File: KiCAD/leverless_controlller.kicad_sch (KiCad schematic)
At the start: 1 part

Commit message: Start PCB Layout
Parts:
- S1: footprint keyswitches.pretty-2.1:Stabilizer_MX_2u -> Fightstick_Library:Kailh_MX_Style_Keyswitch
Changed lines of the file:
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@@
-(kicad_sch (version 20230121) (generator eeschema)
-  (paper "A4")
-  (symbol (lib_id "Keyboard:Stabilizer_MX_2u") (at 49.53 149.86 0) (unit 1)
-    (in_bom no) (on_board yes) (dnp no) (fields_autoplaced)
-    (property "Reference" "S1" (at 59.69 154.305 0)
-      (effects (font (size 1.27 1.27)) (justify left))
-    )
-    (property "Value" "~" (at 49.53 149.86 0)
-      (effects (font (size 1.27 1.27)))
-    )
-    (property "Footprint" "keyswitches.pretty-2.1:Stabilizer_MX_2u" (at 49.53 149.86 0)
-      (effects (font (size 1.27 1.27)) hide)
-    )
-    (property "Datasheet" "" (at 49.53 149.86 0)
-      (effects (font (size 1.27 1.27)) hide)
-    )
-    (instances
-      (project "leverless_controlller"
-        (path "/d4101bc9-65c8-46ec-b973-5d64e4a94ac0"
-          (reference "S1") (unit 1)
-        )
-      )
-    )
-  )
-  (sheet (at 38.1 27.94) (size 64.77 67.31) (fields_autoplaced)
-    (stroke (width 0.1524) (type solid))
-    (fill (color 0 0 0 0.0000))
-    (property "Sheetname" "Main" (at 38.1 27.2284 0)
-      (effects (font (size 1.27 1.27)) (justify left bottom))
-    )
-    (property "Sheetfile" "Main.kicad_sch" (at 38.1 95.8346 0)
-      (effects (font (size 1.27 1.27)) (justify left top))
-    )
-    (instances
-      (project "leverless_controlller"
-        (path "/d4101bc9-65c8-46ec-b973-5d64e4a94ac0" (page "2"))
-      )
-    )
-  )
-  (sheet (at 142.24 29.21) (size 80.01 62.23) (fields_autoplaced)
-    (stroke (width 0.1524) (type solid))
-    (fill (color 0 0 0 0.0000))
-    (property "Sheetname" "Buttons" (at 142.24 28.4984 0)
-      (effects (font (size 1.27 1.27)) (justify left bottom))
-    )
-    (property "Sheetfile" "Buttons.kicad_sch" (at 142.24 92.0246 0)
-      (effects (font (size 1.27 1.27)) (justify left top))
-    )
-    (instances
-      (project "leverless_controlller"
-        (path "/d4101bc9-65c8-46ec-b973-5d64e4a94ac0" (page "3"))
-      )
-    )
-  )
-  (sheet_instances
-    (path "/" (page "1"))
-  )
+(kicad_sch
+	(version 20231120)
+	(generator "eeschema")
+	(generator_version "8.0")
+	(paper "A4")
+	(symbol
+		(lib_id "Keyboard:Stabilizer_MX_2u")
+		(at 49.53 149.86 0)
+		(unit 1)
+		(exclude_from_sim no)
+		(in_bom no)
+		(on_board yes)
+		(dnp no)
+		(fields_autoplaced yes)
+		(property "Reference" "S1"
+			(at 59.69 154.305 0)
+			(effects
+				(font
+					(size 1.27 1.27)
+				)
+				(justify left)
+			)
+		)
+		(property "Value" "~"
+			(at 49.53 149.86 0)
+			(effects
+				(font
+					(size 1.27 1.27)
+				)
+			)
+		)
+		(property "Footprint" "Fightstick_Library:Kailh_MX_Style_Keyswitch"
+			(at 49.53 149.86 0)
+			(effects
+				(font
+					(size 1.27 1.27)
+				)
+				(hide yes)
+			)
+		)
+		(property "Datasheet" ""
+			(at 49.53 149.86 0)
+			(effects
+				(font
+					(size 1.27 1.27)
+				)
+				(hide yes)
+			)
+		)
+		(property "Description" ""
+			(at 49.53 149.86 0)
+			(effects
+				(font
+					(size 1.27 1.27)
+				)
+				(hide yes)
+			)
+		)
+		(instances
+			(project "leverless_controlller"
+				(path "/d4101bc9-65c8-46ec-b973-5d64e4a94ac0"
+					(reference "S1")
+					(unit 1)
+				)
+			)
+		)
+	)
+	(sheet
+		(at 38.1 27.94)
+		(size 64.77 67.31)
+		(fields_autoplaced yes)
+		(stroke
+			(width 0.1524)
+			(type solid)
+		)
+		(fill
+			(color 0 0 0 0.0000)
+		)
+		(property "Sheetname" "Main"
+			(at 38.1 27.2284 0)
+			(effects
+				(font
+					(size 1.27 1.27)
+				)
+				(justify left bottom)
+			)
+		)
+		(property "Sheetfile" "Main.kicad_sch"
+			(at 38.1 95.8346 0)
+			(effects
+				(font
+					(size 1.27 1.27)
+				)
+				(justify left top)
+			)
+		)
+		(instances
+			(project "leverless_controlller"
+				(path "/d4101bc9-65c8-46ec-b973-5d64e4a94ac0"
+					(page "2")
+				)
+			)
+		)
+	)
+	(sheet
+		(at 142.24 29.21)
+		(size 80.01 62.23)
+		(fields_autoplaced yes)
+		(stroke
+			(width 0.1524)
+			(type solid)
+		)
+		(fill
+			(color 0 0 0 0.0000)
+		)
+		(property "Sheetname" "Buttons"
+			(at 142.24 28.4984 0)
+			(effects
+				(font
+					(size 1.27 1.27)
+				)
+				(justify left bottom)
+			)
+		)
+		(property "Sheetfile" "Buttons.kicad_sch"
+			(at 142.24 92.0246 0)
+			(effects
+				(font
+					(size 1.27 1.27)
+				)
+				(justify left top)
+			)
+		)
+		(instances
+			(project "leverless_controlller"
+				(path "/d4101bc9-65c8-46ec-b973-5d64e4a94ac0"
+					(page "3")
+				)
+			)
+		)
+	)
+	(sheet_instances
+		(path "/"
+			(page "1")
+		)
+	)
 )

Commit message: PCB First Draft
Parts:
- S1: footprint Fightstick_Library:Kailh_MX_Style_Keyswitch -> PCM_Mounting_Keyboard_Stabilizer:Stabilizer_Cherry_MX_2.00u
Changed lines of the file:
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@@
 			)
 		)
-		(property "Footprint" "Fightstick_Library:Kailh_MX_Style_Keyswitch"
+		(property "Footprint" "PCM_Mounting_Keyboard_Stabilizer:Stabilizer_Cherry_MX_2.00u"
 			(at 49.53 149.86 0)
 			(effects

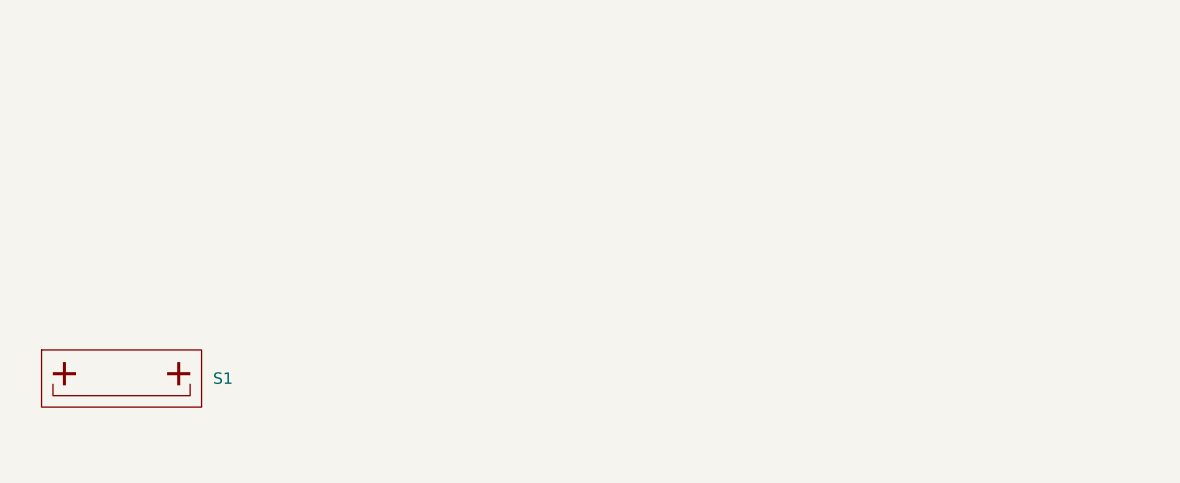
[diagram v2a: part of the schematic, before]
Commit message: Make PCB and case fit together
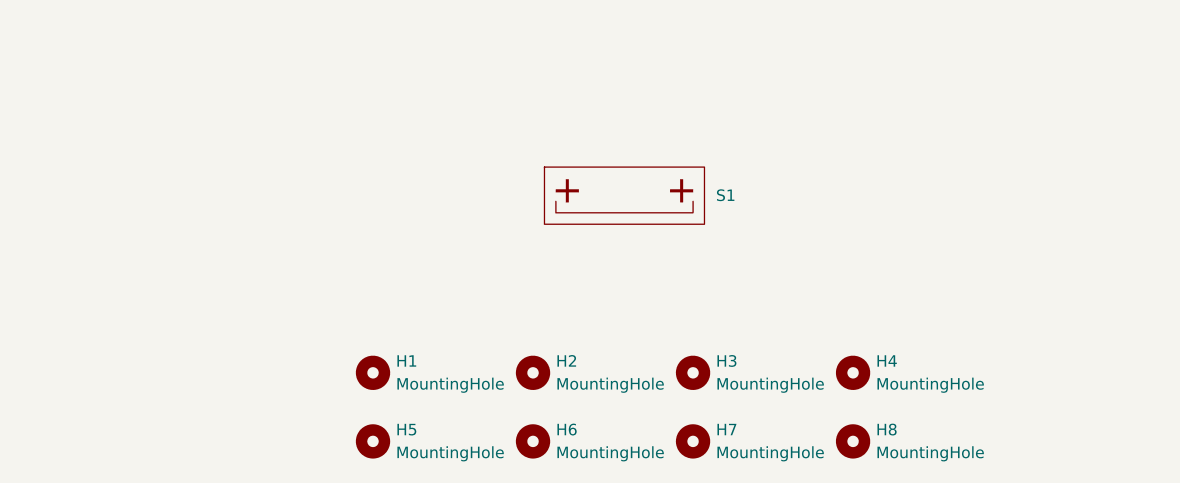
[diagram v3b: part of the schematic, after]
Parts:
- added H1, H2, H3, H4, H5, H6, H7, H8: MountingHole, MountingHole:MountingHole_3.2mm_M3, symbol Mechanical:MountingHole
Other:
- moved on the sheet: S1

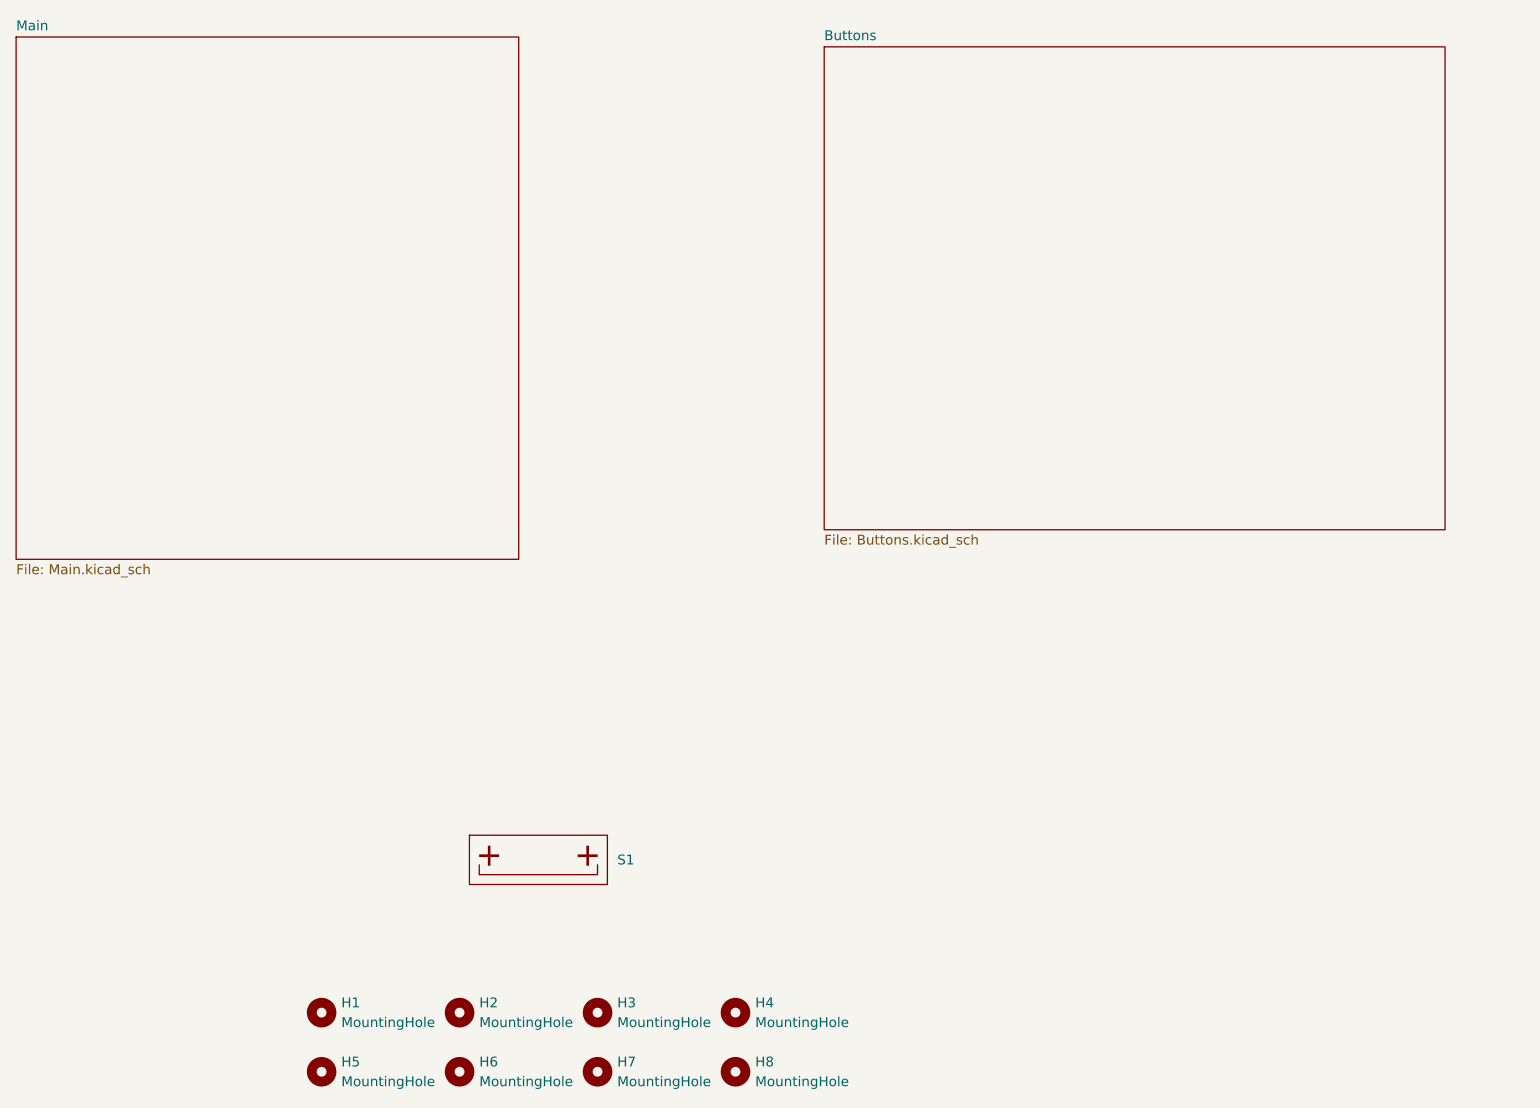
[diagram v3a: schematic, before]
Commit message: Add multiboard configurations
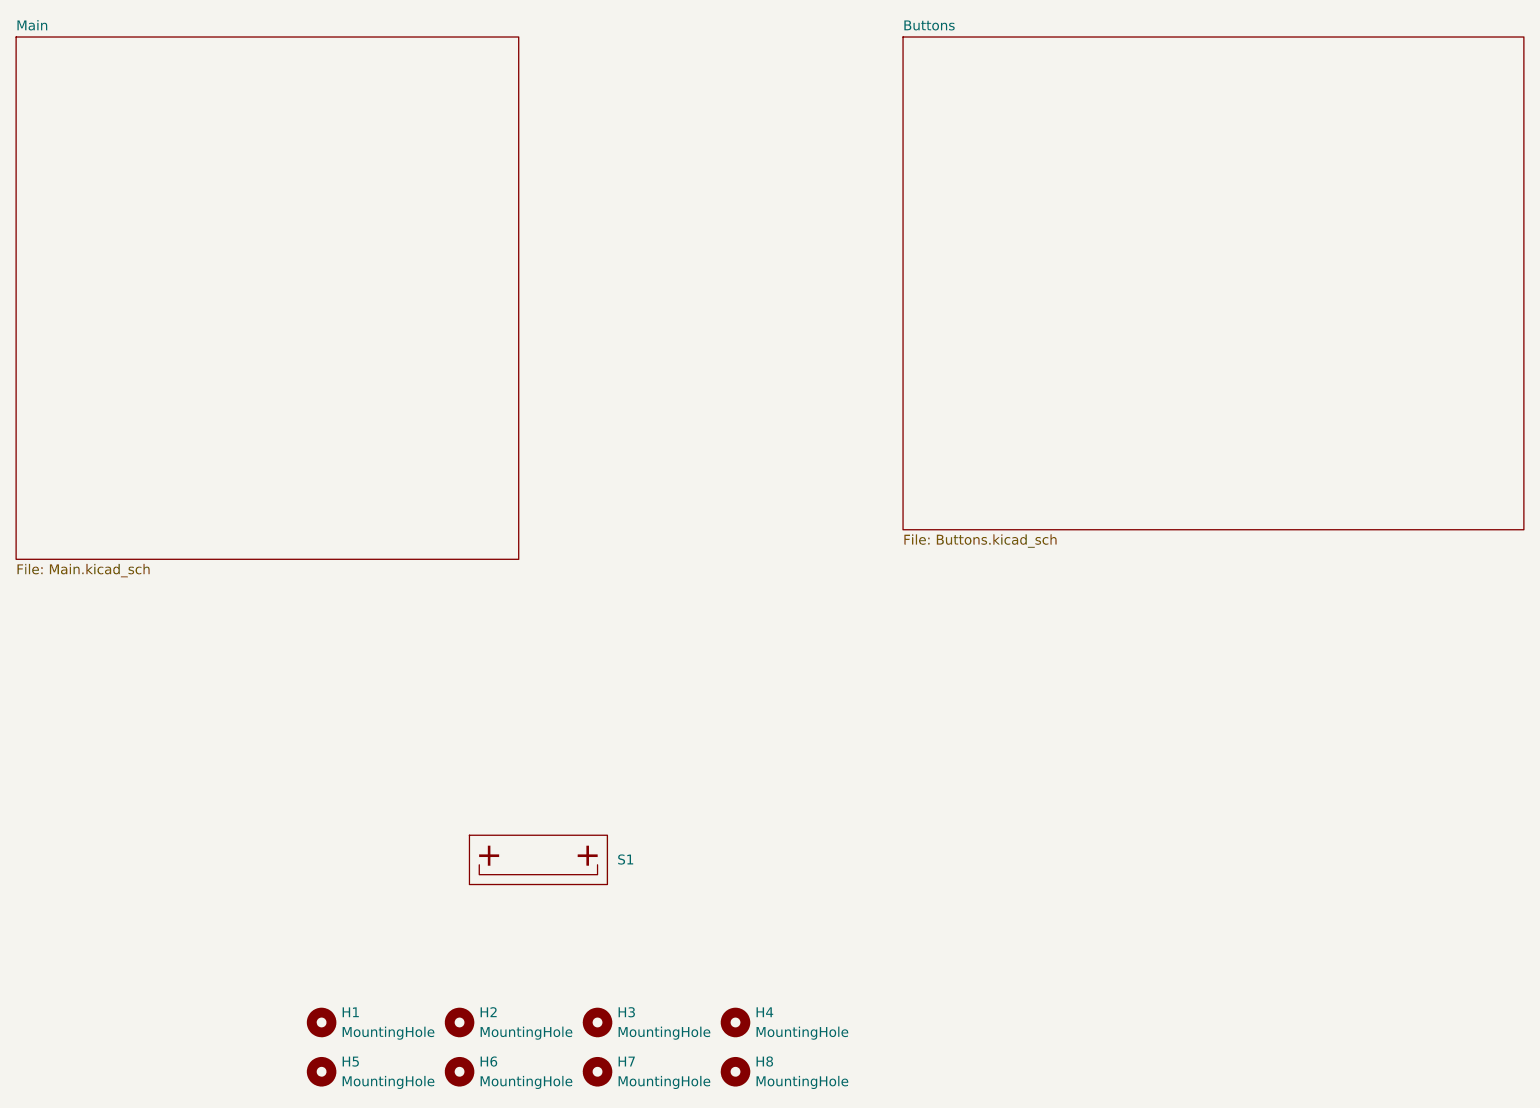
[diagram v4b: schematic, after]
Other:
- moved on the sheet: H1, H2, H3, H4
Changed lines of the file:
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@@
 	(symbol
 		(lib_id "Mechanical:MountingHole")
-		(at 130.81 153.67 0)
+		(at 130.81 154.94 0)
 		(unit 1)
 		(exclude_from_sim yes)
@@
 		(fields_autoplaced yes)
 		(property "Reference" "H4"
-			(at 133.35 152.3999 0)
+			(at 133.35 153.6699 0)
 			(effects
 				(font
@@
 		)
 		(property "Value" "MountingHole"
-			(at 133.35 154.9399 0)
+			(at 133.35 156.2099 0)
 			(effects
 				(font
@@
 		)
 		(property "Footprint" "MountingHole:MountingHole_3.2mm_M3"
-			(at 130.81 153.67 0)
+			(at 130.81 154.94 0)
 			(effects
 				(font
@@
 		)
 		(property "Datasheet" "~"
-			(at 130.81 153.67 0)
+			(at 130.81 154.94 0)
 			(effects
 				(font
@@
 		)
 		(property "Description" "Mounting Hole without connection"
-			(at 130.81 153.67 0)
+			(at 130.81 154.94 0)
 			(effects
 				(font
@@
 	(symbol
 		(lib_id "Mechanical:MountingHole")
-		(at 95.25 153.67 0)
+		(at 95.25 154.94 0)
 		(unit 1)
 		(exclude_from_sim yes)
@@
 		(fields_autoplaced yes)
 		(property "Reference" "H2"
-			(at 97.79 152.3999 0)
+			(at 97.79 153.6699 0)
 			(effects
 				(font
@@
 		)
 		(property "Value" "MountingHole"
-			(at 97.79 154.9399 0)
+			(at 97.79 156.2099 0)
 			(effects
 				(font
@@
 		)
 		(property "Footprint" "MountingHole:MountingHole_3.2mm_M3"
-			(at 95.25 153.67 0)
+			(at 95.25 154.94 0)
 			(effects
 				(font
@@
 		)
 		(property "Datasheet" "~"
-			(at 95.25 153.67 0)
+			(at 95.25 154.94 0)
 			(effects
 				(font
@@
 		)
 		(property "Description" "Mounting Hole without connection"
-			(at 95.25 153.67 0)
+			(at 95.25 154.94 0)
 			(effects
 				(font
@@
 	(symbol
 		(lib_id "Mechanical:MountingHole")
-		(at 77.47 153.67 0)
+		(at 77.47 154.94 0)
 		(unit 1)
 		(exclude_from_sim yes)
@@
 		(fields_autoplaced yes)
 		(property "Reference" "H1"
-			(at 80.01 152.3999 0)
+			(at 80.01 153.6699 0)
 			(effects
 				(font
@@
 		)
 		(property "Value" "MountingHole"
-			(at 80.01 154.9399 0)
+			(at 80.01 156.2099 0)
 			(effects
 				(font
@@
 		)
 		(property "Footprint" "MountingHole:MountingHole_3.2mm_M3"
-			(at 77.47 153.67 0)
+			(at 77.47 154.94 0)
 			(effects
 				(font
@@
 		)
 		(property "Datasheet" "~"
-			(at 77.47 153.67 0)
+			(at 77.47 154.94 0)
 			(effects
 				(font
@@
 		)
 		(property "Description" "Mounting Hole without connection"
-			(at 77.47 153.67 0)
+			(at 77.47 154.94 0)
 			(effects
 				(font
@@
 	(symbol
 		(lib_id "Mechanical:MountingHole")
-		(at 113.03 153.67 0)
+		(at 113.03 154.94 0)
 		(unit 1)
 		(exclude_from_sim yes)
@@
 		(fields_autoplaced yes)
 		(property "Reference" "H3"
-			(at 115.57 152.3999 0)
+			(at 115.57 153.6699 0)
 			(effects
 				(font
@@
 		)
 		(property "Value" "MountingHole"
-			(at 115.57 154.9399 0)
+			(at 115.57 156.2099 0)
 			(effects
 				(font
@@
 		)
 		(property "Footprint" "MountingHole:MountingHole_3.2mm_M3"
-			(at 113.03 153.67 0)
+			(at 113.03 154.94 0)
 			(effects
 				(font
@@
 		)
 		(property "Datasheet" "~"
-			(at 113.03 153.67 0)
+			(at 113.03 154.94 0)
 			(effects
 				(font
@@
 		)
 		(property "Description" "Mounting Hole without connection"
-			(at 113.03 153.67 0)
+			(at 113.03 154.94 0)
 			(effects
 				(font
@@
 	)
 	(sheet
-		(at 142.24 29.21)
-		(size 80.01 62.23)
+		(at 152.4 27.94)
+		(size 80.01 63.5)
 		(fields_autoplaced yes)
 		(stroke
@@
 		)
 		(property "Sheetname" "Buttons"
-			(at 142.24 28.4984 0)
+			(at 152.4 27.2284 0)
 			(effects
 				(font
@@
 		)
 		(property "Sheetfile" "Buttons.kicad_sch"
-			(at 142.24 92.0246 0)
-			(effects
-				(font
+			(at 152.4 92.0246 0)
+			(effects
+				(font
